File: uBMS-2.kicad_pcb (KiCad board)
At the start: 4 copper layers, 60 x 90 mm, 179 parts, among them J1 Conn_02x03_Counter_Clockwise, J2 Conn_01x02, J3 Conn_01x01, J4 Conn_01x01, J5 Conn_02x07_Counter_Clockwise, J6 Conn_02x07_Counter_Clockwise, J7 Conn_02x07_Counter_Clockwise, J8 Conn_01x01, Q1 2N7002, Q10 FQD5N20L, Q11 FQD5N20L, Q12 FQD5N20L, Q13 FQD5N20L, Q14 FQD5N20L, Q15 FQD5N20L, Q2 2N7002, Q3 NTD5865NL, Q4 FQD5N20L, Q5 FQD5N20L, Q6 FQD5N20L, Q7 FQD5N20L, Q8 FQD5N20L, Q9 FQD5N20L, U1 LM2576HVS-5, U10 CD74HC4067SM, U11 CD74HC4067SM, U2 ADS1115IDGS, U3 TLV1117-33, U4 TL431DBV, U5 ESP32-WROOM-32, U6 TSC2012IDT, U7 MCP23017_SS, U8 MCP23008-E_P, U9 VDMG10C0

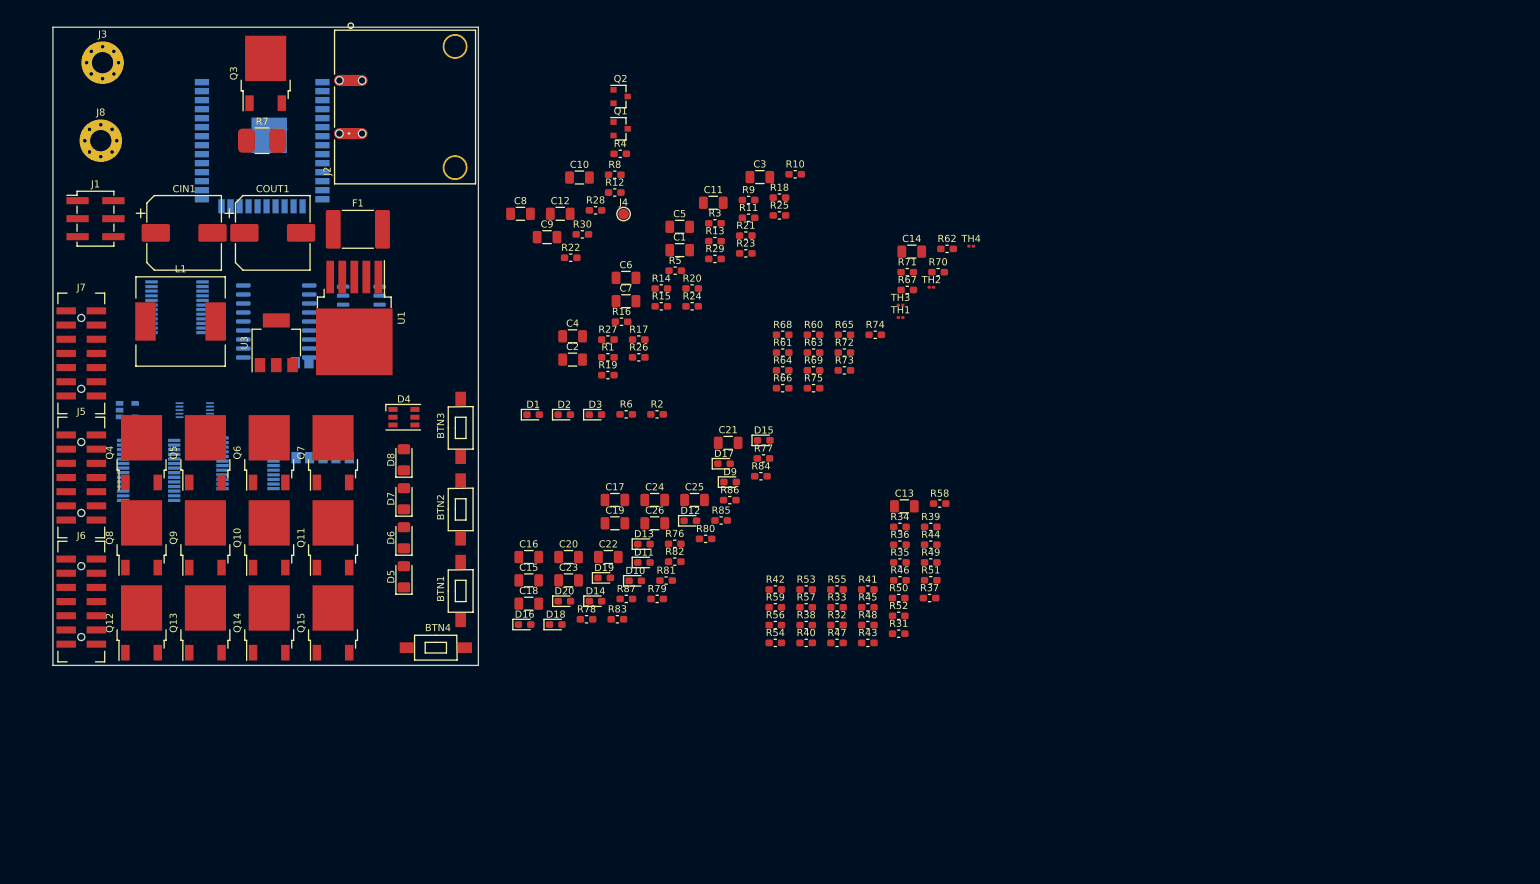
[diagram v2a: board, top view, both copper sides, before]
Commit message: Laid out Balance Circuitry
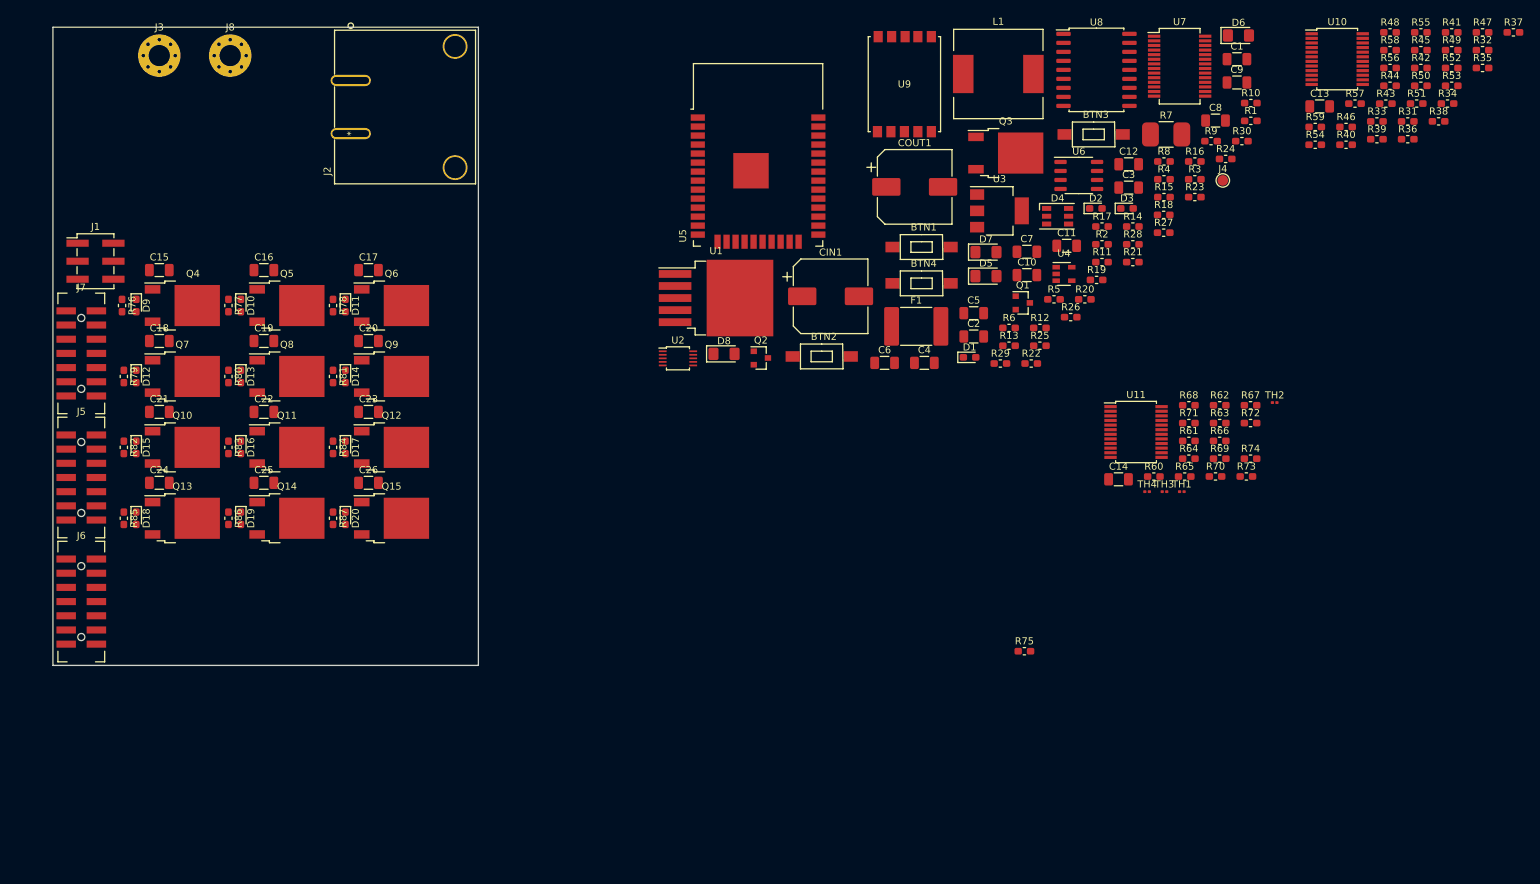
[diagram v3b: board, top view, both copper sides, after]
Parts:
- U10, U11, U2, U4, U5, U6, U7, U8, U9: moved to F.Cu
- moved U10 167.3 mm to (201.1, 24.5)
- moved U7 156.2 mm to (178.9, 25.5)
- moved D6 137.4 mm to (187.2, 21.2), turned to 0 degrees
- moved U4 133.5 mm to (162.6, 54.8)
- moved R7 127.5 mm to (177.0, 35.1)
- moved U11 125.3 mm to (172.7, 77.1)
- moved R47 125.3 mm to (221.6, 20.7)
- moved R32 121.9 mm to (221.6, 23.2)
- moved U8 121.0 mm to (167.2, 26.0)
- moved L1 120.5 mm to (153.3, 26.6)
- moved R42 117.0 mm to (212.9, 25.7)
- moved R56 117.0 mm to (208.6, 25.7)
- moved R53 115.5 mm to (217.3, 28.3)
- moved R37 114.7 mm to (226.0, 20.7)
- moved R38 114.0 mm to (215.4, 33.3)
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
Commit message: Added rounded corners and 2mm mounting holes
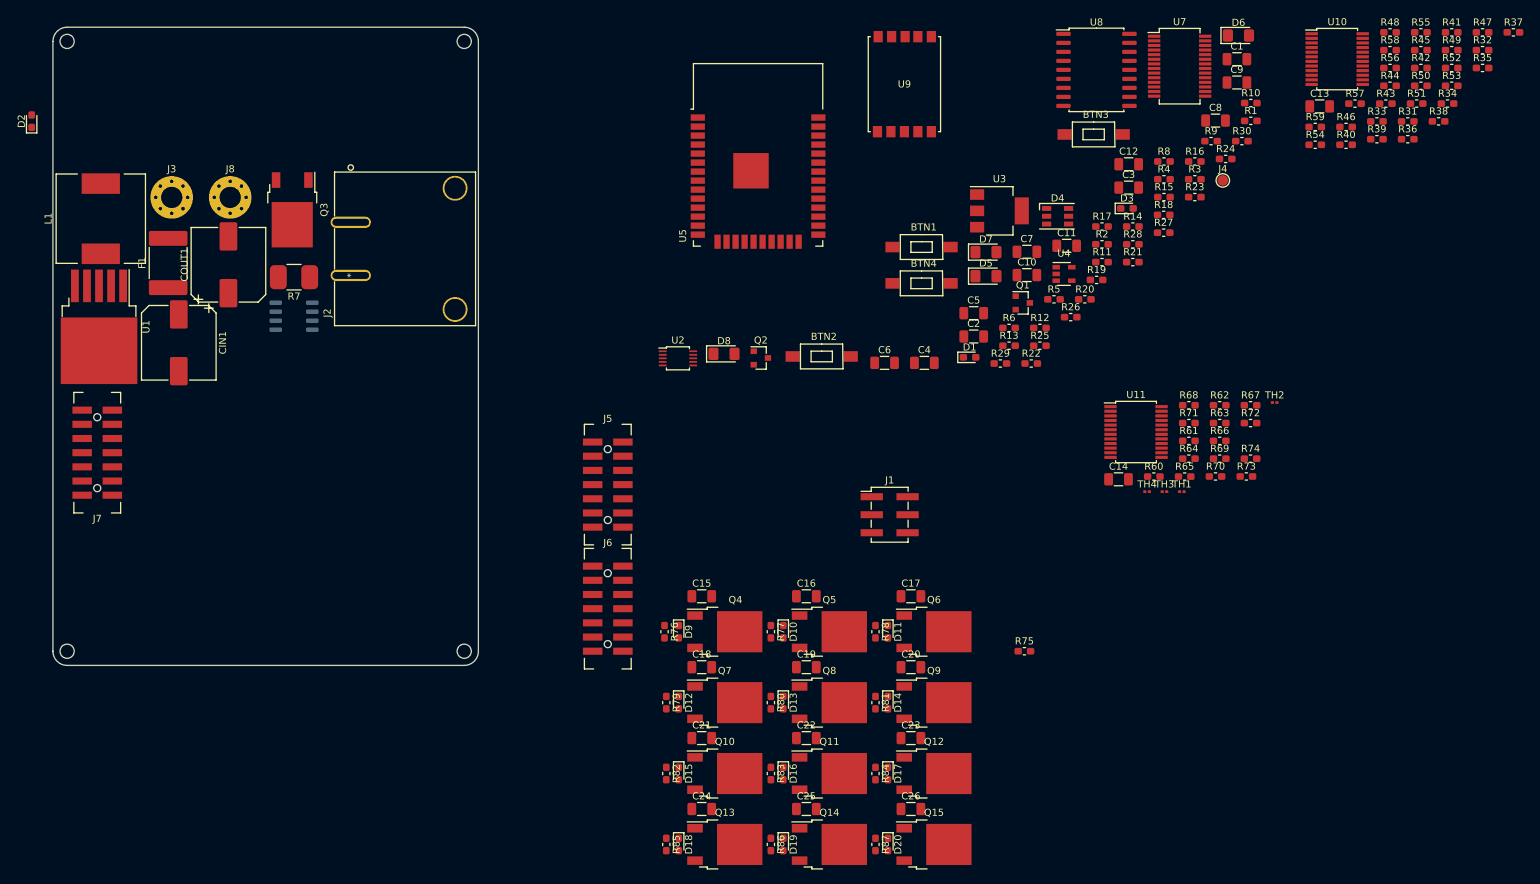
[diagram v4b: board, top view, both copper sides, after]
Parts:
- added H1: MountingHole, MountingHole:MountingHole_2mm, F.Cu at (22.0, 22.0)
- added H2: MountingHole, MountingHole:MountingHole_2mm, F.Cu at (78.0, 22.0)
- added H3: MountingHole, MountingHole:MountingHole_2mm, F.Cu at (22.0, 108.0)
- added H4: MountingHole, MountingHole:MountingHole_2mm, F.Cu at (78.0, 108.0)
- U6: moved to B.Cu
- moved D2 150.6 mm to (17.0, 33.2), turned to 90 degrees
- moved L1 128.2 mm to (26.8, 47.0), turned to 90 degrees
- moved R7 124.6 mm to (54.0, 55.2), turned to 180 degrees
- moved J1 117.6 mm to (138.0, 88.8)
- moved U6 112.4 mm to (54.0, 60.8), turned to 180 degrees
- moved F1 105.9 mm to (36.2, 53.2), turned to 90 degrees
- moved Q3 100.9 mm to (53.8, 45.8), turned to 270 degrees
- moved COUT1 97.4 mm to (44.8, 53.5), turned to 90 degrees
- moved CIN1 92.2 mm to (37.8, 64.5), turned to 270 degrees
- moved C15 89.3 mm to (111.5, 100.2)
- moved C16 89.3 mm to (126.2, 100.2)
- moved C17 89.3 mm to (141.0, 100.2)
- moved C18 89.3 mm to (111.5, 110.2)
- moved C19 89.3 mm to (126.2, 110.2)
- moved C20 89.3 mm to (141.0, 110.2)
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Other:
- outline, holes or cut-outs redrawn

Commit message: Laid out components on PCB in semi-final state
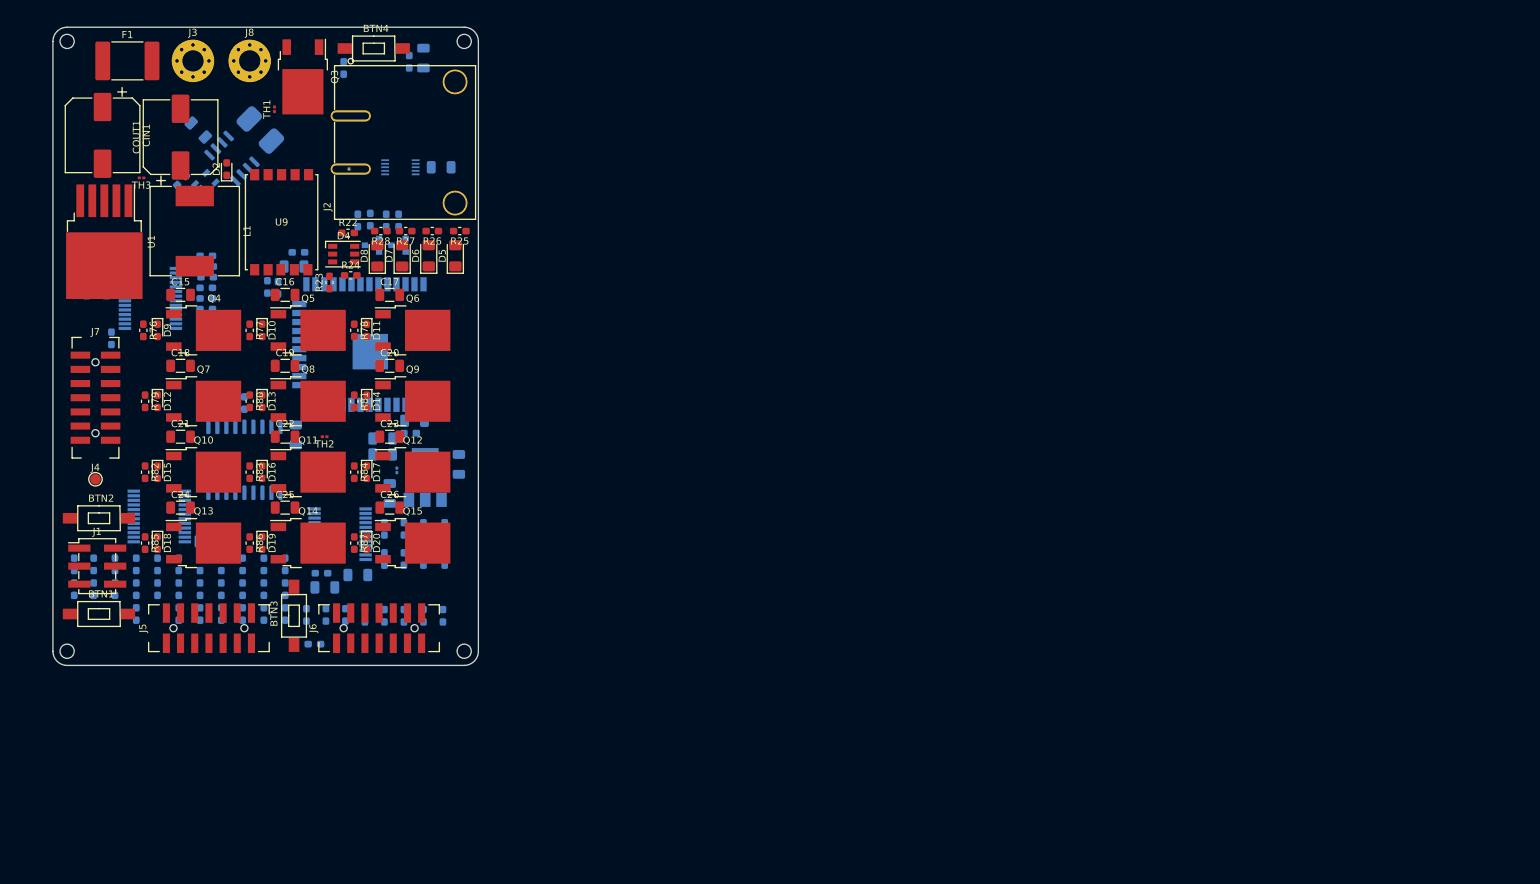
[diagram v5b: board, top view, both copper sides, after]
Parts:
- C1, C10, C11, C12, C13, C14, C2, C3, C4, C5, C6, C7, C8, C9, D1, D3, Q1, Q2, R1, R10, R11, R12, R13, R14, R15, R16, R17, R18, R19, R2, R20, R21, R29, R3, R30, R31, R32, R33, R34, R35, R36, R37, R38, R39, R4, R40, R41, R42, R43, R44, R45, R46, R47, R48, R49, R5, R50, R51, R52, R53, R54, R55, R56, R57, R58, R59, R6, R60, R61, R62, R63, R64, R65, R66, R67, R68, R69, R7, R70, R71, R72, R73, R74, R75, R8, R9, TH4, U10, U11, U2, U3, U4, U5, U7, U8: moved to B.Cu
- moved R37 216.4 mm to (23.0, 95.8), turned to 90 degrees
- moved R32 210.1 mm to (25.8, 99.2), turned to 90 degrees
- moved R35 200.8 mm to (34.8, 99.2), turned to 90 degrees
- moved R38 199.7 mm to (25.8, 95.8), turned to 90 degrees
- moved R31 199.3 mm to (23.0, 99.2), turned to 90 degrees
- moved R34 198.4 mm to (31.8, 102.8), turned to 90 degrees
- moved R41 197.3 mm to (34.8, 95.8), turned to 90 degrees
- moved R47 193.1 mm to (46.8, 102.8), turned to 90 degrees
- moved R42 190.0 mm to (37.8, 99.2), turned to 90 degrees
- moved R33 189.8 mm to (28.8, 99.2), turned to 90 degrees
- moved R45 189.6 mm to (40.8, 102.8), turned to 90 degrees
- moved R52 188.4 mm to (43.8, 99.2), turned to 90 degrees
- moved R43 187.8 mm to (31.8, 95.8), turned to 90 degrees
- moved R55 187.8 mm to (40.8, 95.8), turned to 90 degrees
- moved R39 187.8 mm to (28.8, 95.8), turned to 90 degrees
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
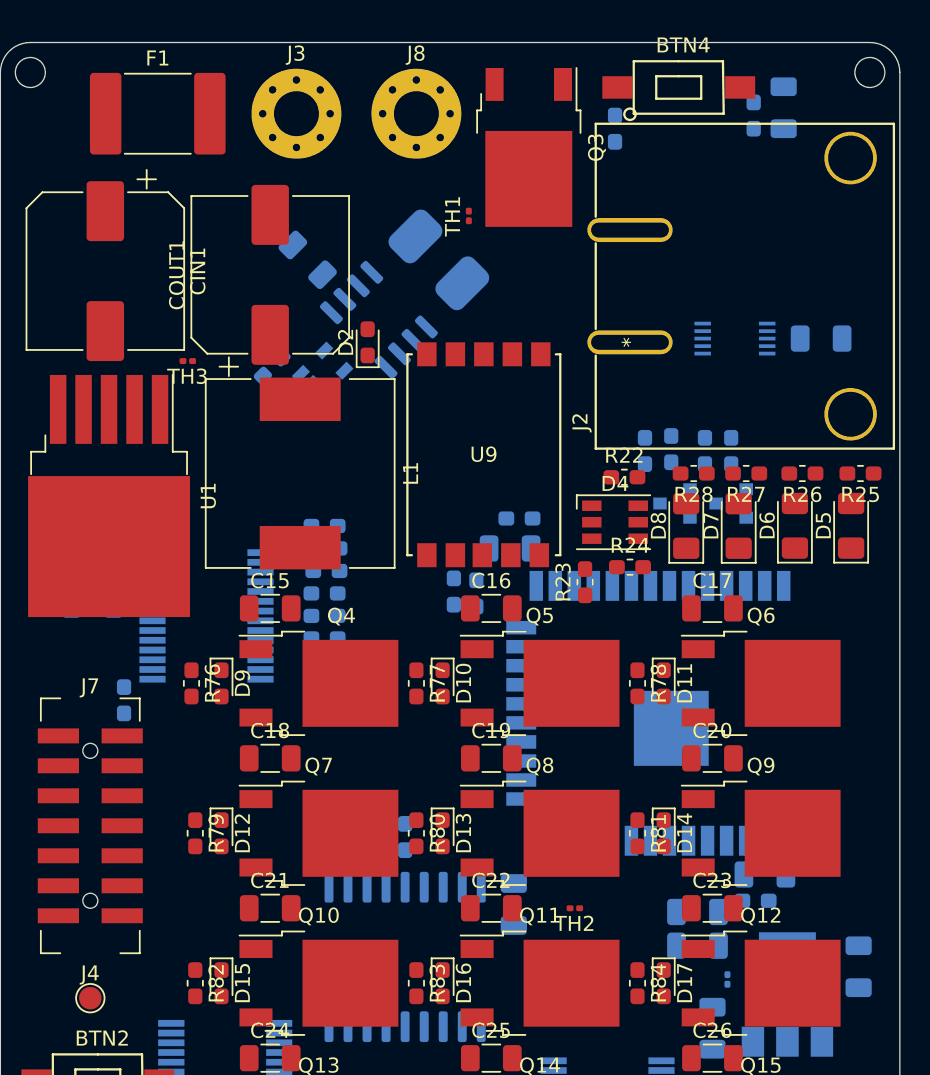
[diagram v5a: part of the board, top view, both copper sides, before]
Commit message: Fixed volt reg footprint, fill power planes, added high current paths
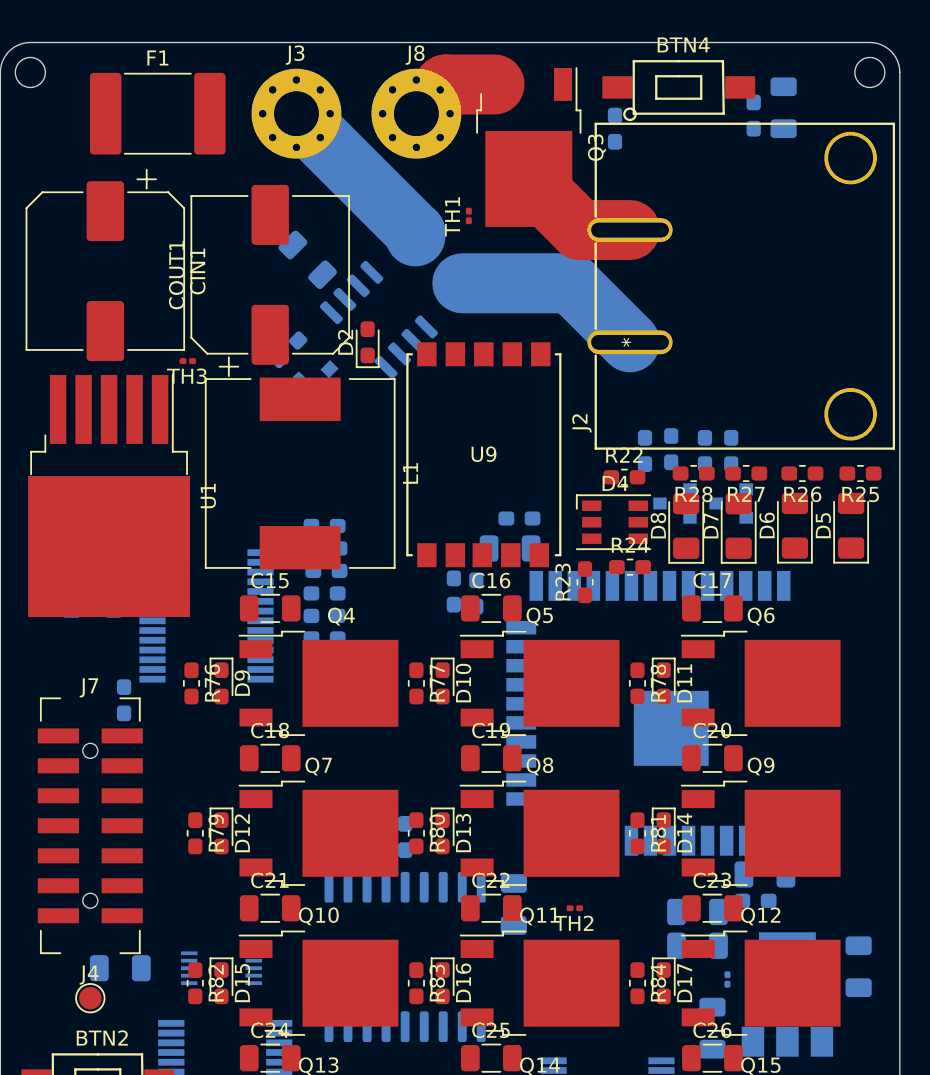
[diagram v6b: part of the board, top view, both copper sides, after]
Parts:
- U4: footprint Package_TO_SOT_SMD:SOT-23-5 -> Package_TO_SOT_SMD:SOT-23
- moved C1 62.8 mm to (28.0, 81.8), turned to 180 degrees
- moved U2 54.2 mm to (34.8, 81.8), turned to 180 degrees
- moved R8 1.58 mm to (39.2, 40.5)
- moved U4 0.56 mm to (41.2, 42.5)
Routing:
- net /SYS_Pos: track 0.00 -> 12.8 mm
- net /Batt_Pos: track 0.00 -> 11.5 mm
- net /SYS_RTN: track 0.00 -> 8.16 mm
- net GND: track 0.00 -> 6.03 mm
- added copper zone on In2.Cu, net +5V
- added copper zone on In1.Cu, net GND

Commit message: routed and filled a bunch of stuff, so much more to do
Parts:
- J5, J6, J7: value Conn_02x07_Counter_Clockwise -> Conn_02x07_Odd_Even; footprint uBMS-2:Molex_Milli_Grid_0878325623 -> uBMS-2:Molex_Milli_Grid_0878325623_TopBottom
- U4: value TL431DBV -> TL431DBZ
- moved C6 70.6 mm to (28.4, 26.9), turned to 0 degrees
- moved U3 66.4 mm to (30.7, 31.9), turned to 0 degrees
- moved C7 66.2 mm to (28.6, 36.8), turned to 180 degrees
- moved TH4 66.1 mm to (31.6, 27.7), turned to 0 degrees
- moved C1 40.9 mm to (52.1, 48.7)
- moved U2 39.9 mm to (52.0, 45.7), turned to 0 degrees
- moved C14 32.1 mm to (94.2, 89.6), turned to 0 degrees
- moved R58 26.9 mm to (26.3, 100.4)
- moved R54 26.8 mm to (26.3, 103.7)
- moved R49 26.8 mm to (26.3, 107.0)
- moved R59 25.0 mm to (24.8, 97.1)
- moved R50 25.0 mm to (24.8, 100.4)
- moved R48 24.9 mm to (24.8, 103.7)
- moved R57 24.9 mm to (21.9, 97.1), turned to 270 degrees
- moved R47 23.5 mm to (23.4, 100.4)
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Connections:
- J6 pad 1: +5V -> /TempMultiplex/CellTemp_1
- J6 pad 10: /TempMultiplex/CellTemp_9 -> /TempMultiplex/CellTemp_10
- J6 pad 11: /TempMultiplex/CellTemp_10 -> /TempMultiplex/CellTemp_11
- J6 pad 12: /TempMultiplex/CellTemp_11 -> /TempMultiplex/CellTemp_12
- J6 pad 13: /TempMultiplex/CellTemp_12 -> +5V
- J6 pad 2: /TempMultiplex/CellTemp_1 -> /TempMultiplex/CellTemp_2
- J6 pad 3: /TempMultiplex/CellTemp_2 -> /TempMultiplex/CellTemp_3
- J6 pad 4: /TempMultiplex/CellTemp_3 -> /TempMultiplex/CellTemp_4
- J6 pad 5: /TempMultiplex/CellTemp_4 -> /TempMultiplex/CellTemp_5
- J6 pad 6: /TempMultiplex/CellTemp_5 -> /TempMultiplex/CellTemp_6
- J6 pad 7: /TempMultiplex/CellTemp_6 -> /TempMultiplex/CellTemp_7
- J6 pad 8: /TempMultiplex/CellTemp_7 -> /TempMultiplex/CellTemp_8
- J6 pad 9: /TempMultiplex/CellTemp_8 -> /TempMultiplex/CellTemp_9
- U4 pad 1: (no net) -> /REF_2.5
- U4 pad 2: (no net) -> /REF_2.5
- U4 pad 3: /REF_2.5 -> GND
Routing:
- net +3V3: track 0.00 -> 116.6 mm, vias 0 -> 6
- net GND: track 6.03 -> 92.8 mm, vias 0 -> 11
- net /BatteryBalance/Cell6_P: track 0.00 -> 75.6 mm, vias 0 -> 3
- net /BatteryBalance/Cell3_P: track 0.00 -> 68.6 mm, vias 0 -> 3
- net /BatteryBalance/Cell9_P: track 0.00 -> 66.7 mm, vias 0 -> 2
- net /BatteryBalance/Cell2_P: track 0.00 -> 65.5 mm, vias 0 -> 2
- net /BatteryBalance/Cell11_P: track 0.00 -> 60.4 mm, vias 0 -> 2
- net /BatteryBalance/Cell8_P: track 0.00 -> 60.1 mm, vias 0 -> 2
- net /BatteryBalance/Cell5_P: track 0.00 -> 53.2 mm, vias 0 -> 2
- net /BatteryBalance/Cell10_P: track 0.00 -> 52.9 mm, vias 0 -> 2
- net /BatteryBalance/Cell12_P: track 0.00 -> 50.2 mm, vias 0 -> 2
- net +5V: track 0.00 -> 46.8 mm, vias 0 -> 3
- net /BatteryBalance/Cell7_P: track 0.00 -> 42.3 mm, vias 0 -> 4
- net /BatteryBalance/Cell4_P: track 0.00 -> 41.5 mm, vias 0 -> 2
- net /BatteryBalance/Cell1_P: track 0.00 -> 40.8 mm, vias 0 -> 2
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- added copper zone on B.Cu, net +3V3
- added copper zone on B.Cu, net /Batt_Pos
- added copper zone on F.Cu, net /Batt_Pos
- added copper zone on B.Cu, net /SYS_Pos
- added copper zone on F.Cu, net /SYS_RTN
- added copper zone on F.Cu, net GND
- removed copper zone on In2.Cu, net +5V
